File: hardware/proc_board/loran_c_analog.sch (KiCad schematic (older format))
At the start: 55 parts, among them P601 DAC VCO, P602 DAC AGC, P603 QUAD In, P604 LORAN In, Q601 BD135, Q602 BD136, U601 TL072, U602 LD1117S33

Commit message: Update: fixed AGND zone on PCB
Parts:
- P603: footprint (none) -> w_conn_kk100:kk100_22-23-2041
- Q601, Q602: footprint Housings_SOT:SOT126_SOT32_Housing_Horizontal_RevA_22Oct2012 -> Housings_SOT:SOT126_SOT32_Housing_Vertical_BigPads
- R603, R604: footprint w_pth_resistors:RC07 -> w_pth_resistors:RC05
- R605, R606: footprint w_smd_resistors:r_1206 -> w_smd_resistors:r_0805
- U601: footprint w_pth_ic:dil_8-300 -> w_smd_dil:so-8
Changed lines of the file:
@@
 F 0 "R603" V 3080 1550 40  0000 C CNN
 F 1 "330 0.5W" V 3007 1551 40  0000 C CNN
-F 2 "w_pth_resistors:RC07" V 2930 1550 30  0001 C CNN
+F 2 "w_pth_resistors:RC05" V 2930 1550 30  0001 C CNN
 F 3 "" H 3000 1550 30  0000 C CNN
 	1    3000 1550
@@
 F 0 "Q601" H 3700 1250 40  0000 R CNN
 F 1 "BD135" H 3700 1550 40  0000 R CNN
-F 2 "Housings_SOT:SOT126_SOT32_Housing_Horizontal_RevA_22Oct2012" H 3580 1500 29  0001 C CNN
+F 2 "Housings_SOT:SOT126_SOT32_Housing_Vertical_BigPads" H 3580 1500 29  0001 C CNN
 F 3 "" H 3700 1400 60  0000 C CNN
 	1    3700 1400
@@
 F 0 "Q602" H 3700 3150 40  0000 R CNN
 F 1 "BD136" H 3700 3450 40  0000 R CNN
-F 2 "Housings_SOT:SOT126_SOT32_Housing_Horizontal_RevA_22Oct2012" H 3580 3400 29  0001 C CNN
+F 2 "Housings_SOT:SOT126_SOT32_Housing_Vertical_BigPads" H 3580 3400 29  0001 C CNN
 F 3 "" H 3700 3300 60  0000 C CNN
 	1    3700 3300
@@
 F 0 "R604" V 3080 3150 40  0000 C CNN
 F 1 "330 0.5W" V 3007 3151 40  0000 C CNN
-F 2 "w_pth_resistors:RC07" V 2930 3150 30  0001 C CNN
+F 2 "w_pth_resistors:RC05" V 2930 3150 30  0001 C CNN
 F 3 "" H 3000 3150 30  0000 C CNN
 	1    3000 3150
@@
 F 0 "U601" H 2750 5350 60  0000 L CNN
 F 1 "TL072" H 2750 4900 60  0000 L CNN
-F 2 "w_pth_ic:dil_8-300" H 2800 5150 60  0001 C CNN
+F 2 "w_smd_dil:so-8" H 2800 5150 60  0001 C CNN
 F 3 "" H 2800 5150 60  0000 C CNN
 	2    2800 5150
@@
 F 0 "U601" H 2750 6450 60  0000 L CNN
 F 1 "TL072" H 2750 6000 60  0000 L CNN
-F 2 "w_pth_ic:dil_8-300" H 2800 6250 60  0001 C CNN
+F 2 "w_smd_dil:so-8" H 2800 6250 60  0001 C CNN
 F 3 "" H 2800 6250 60  0000 C CNN
 	1    2800 6250
@@
 F 0 "R605" V 4430 5150 40  0000 C CNN
 F 1 "33" V 4357 5151 40  0000 C CNN
-F 2 "w_smd_resistors:r_1206" V 4280 5150 30  0001 C CNN
+F 2 "w_smd_resistors:r_0805" V 4280 5150 30  0001 C CNN
 F 3 "" H 4350 5150 30  0000 C CNN
 	1    4350 5150
@@
 F 0 "R606" V 4430 6250 40  0000 C CNN
 F 1 "33" V 4357 6251 40  0000 C CNN
-F 2 "w_smd_resistors:r_1206" V 4280 6250 30  0001 C CNN
+F 2 "w_smd_resistors:r_0805" V 4280 6250 30  0001 C CNN
 F 3 "" H 4350 6250 30  0000 C CNN
 	1    4350 6250
@@
 F 0 "P603" V 7350 4350 50  0000 C CNN
 F 1 "QUAD In" V 7450 4350 50  0000 C CNN
-F 2 "" H 7400 4350 60  0000 C CNN
+F 2 "w_conn_kk100:kk100_22-23-2041" H 7400 4350 60  0001 C CNN
 F 3 "" H 7400 4350 60  0000 C CNN
 	1    7400 4350

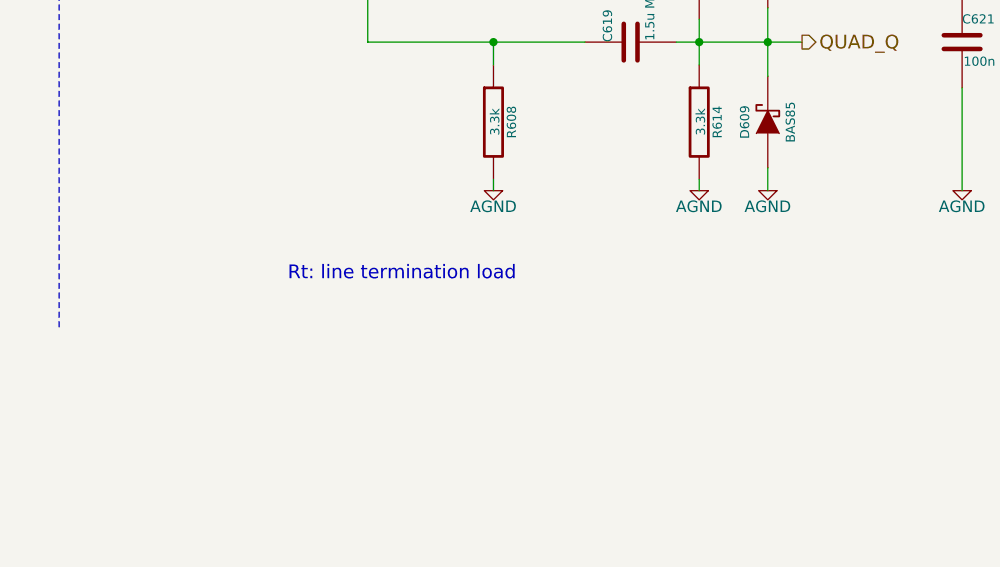
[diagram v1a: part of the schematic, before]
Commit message: PCB prototype production version, minor schematic updates PCB files sent to PCB house. PCB revision as of this commit can be treated as a first (and, hopefully, last) prototype version
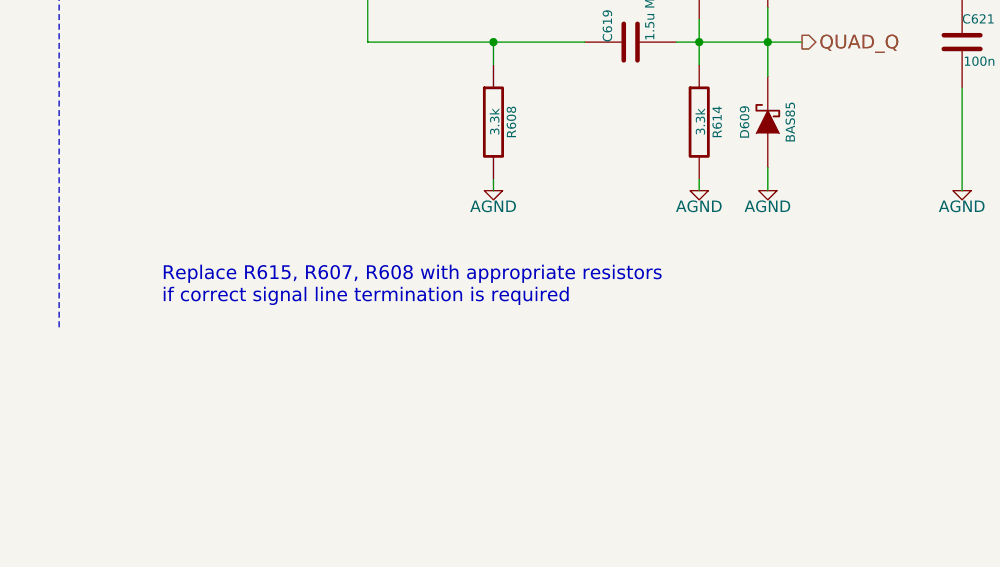
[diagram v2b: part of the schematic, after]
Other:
- note added: "Replace R615, R607, R608 with appropriate resistors\nif correct signal line termination is required"
- note removed: "Rt: line termination load"
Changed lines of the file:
@@
 	1    0    0    -1
 $EndComp
-Text Notes 7900 6300 0    60   ~ 0
-Rt: line termination load
 Text Label 2500 1100 0    60   ~ 0
 +15V_AS
@@
 Wire Notes Line
 	6900 550  6900 6500
+Text Notes 7350 6400 0    60   ~ 0
+Replace R615, R607, R608 with appropriate resistors\nif correct signal line termination is required
 $EndSCHEMATC
